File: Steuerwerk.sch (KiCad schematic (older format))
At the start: 130 parts, among them J1 2PinTerminalBlocktg, J10 2PinTerminalBlocktg, J11 2PinTerminalBlocktg, J12 2PinTerminalBlocktg, J2 2PinTerminalBlocktg, J3 3PinTerminalBlocktg, J4 3PinTerminalBlocktg, J5 2PinTerminalBlocktg, J6 2PinTerminalBlocktg, J7 2PinTerminalBlocktg, J8 2PinTerminalBlocktg, J9 2PinTerminalBlocktg, Q1 Q_PNP_BCE, U1 74ls240, U2 74541, U3 74LS161, U4 74LS138, U5 74LS138, U6 74541, U7 74LS374, U8 74LS374

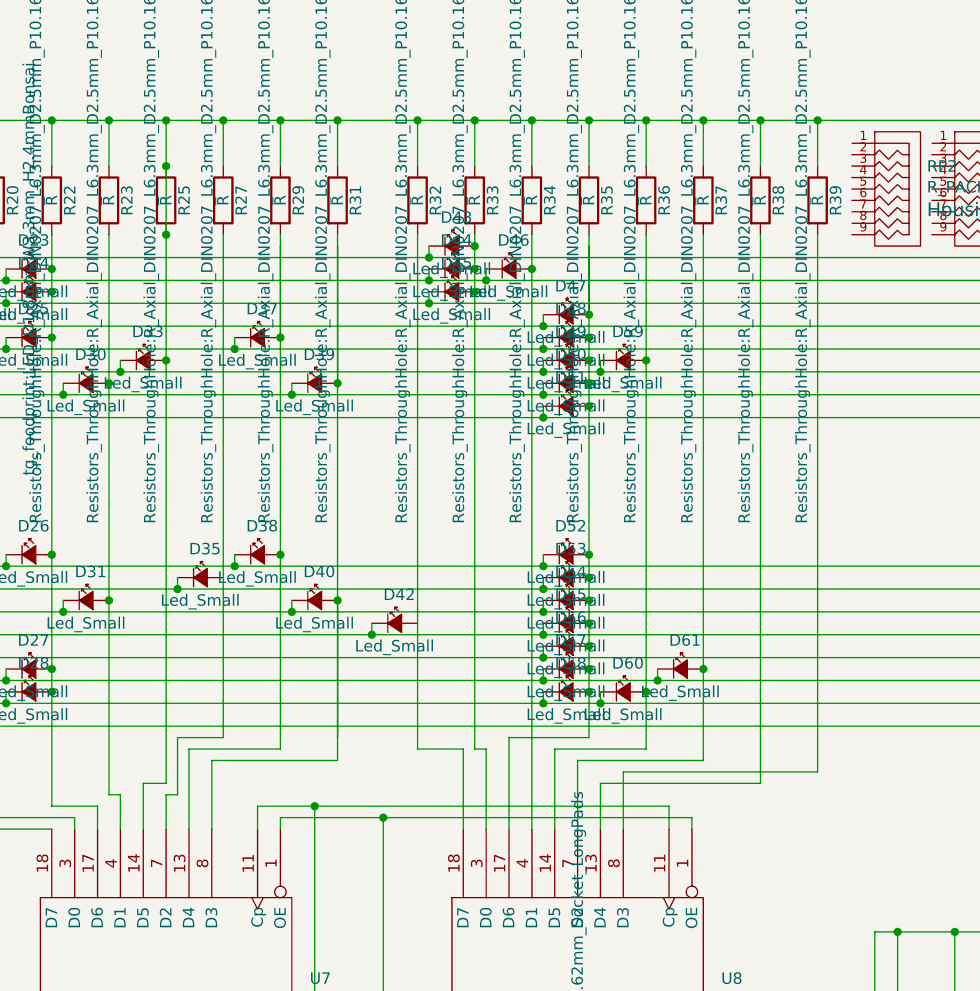
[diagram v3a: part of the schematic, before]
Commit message: Pin Anordnung von 374 korrigiert, manche Fehler gefunden und Todo Liste erweitert
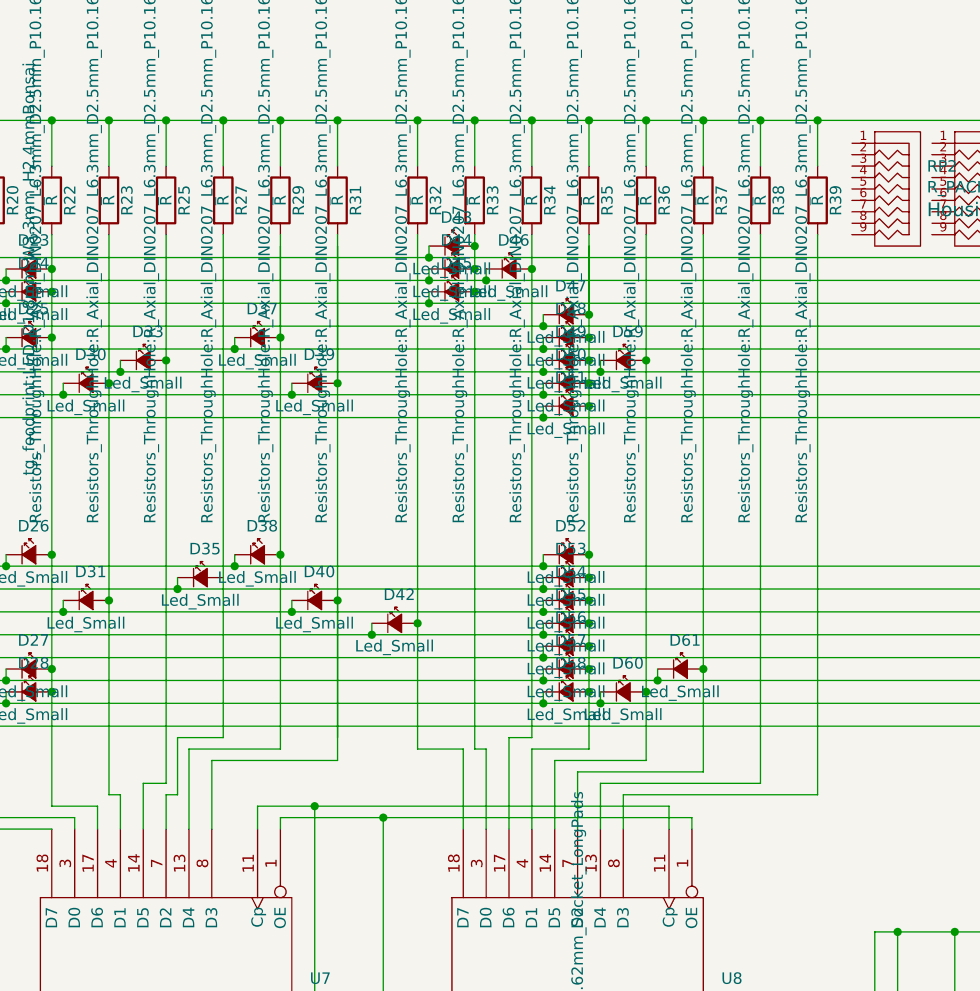
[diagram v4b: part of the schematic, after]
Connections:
- wire segments 441 -> 442
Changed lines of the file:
@@
 	8550 1000 8550 3400
-Wire Wire Line
-	7750 3300 8300 3300
-Wire Wire Line
-	8050 3250 7650 3250
-Wire Wire Line
-	7450 3200 7800 3200
 Wire Wire Line
 	6700 3300 6150 3300
@@
 	6000 2500 6000 2550
 Wire Wire Line
-	8800 1000 8800 3350
-Wire Wire Line
 	5200 1000 5200 1050
 Connection ~ 5200 500
@@
 	3550 700  3550 1100
 Wire Wire Line
-	7950 3350 8800 3350
+	7950 3450 8800 3450
 Wire Wire Line
 	8100 2950 11150 2950
@@
 	7950 5000 7950 6100
 Wire Wire Line
-	7950 3350 7950 3600
-Wire Wire Line
-	7750 3300 7750 3600
-Wire Wire Line
-	7650 3250 7650 3600
-Wire Wire Line
-	7450 3200 7450 3600
-Wire Wire Line
-	7250 3550 7250 3600
-Wire Wire Line
-	7250 3550 7250 3250
-Wire Wire Line
 	7250 3250 7050 3250
 Wire Wire Line
@@
 	6600 3550 6900 3550
 Wire Wire Line
-	7250 3550 8250 3550
-Wire Wire Line
 	6900 5250 6900 3550
 Wire Wire Line
 	1500 5250 6900 5250
-Connection ~ 6900 3550
-Wire Wire Line
-	6900 3550 7250 3550
 Connection ~ 1500 5250
 Wire Wire Line
@@
 Wire Wire Line
 	1050 5250 1500 5250
-Wire Wire Line
-	7050 1000 7050 3250
 Wire Wire Line
 	6200 1000 6200 3200
@@
 Wire Wire Line
 	5700 2600 5700 3450
-Connection ~ 5950 700
-Connection ~ 5950 1000
-Wire Wire Line
-	5950 1000 5950 700
 Wire Wire Line
 	5950 1550 5950 3400
@@
 	6700 1000 6700 1650
 Wire Wire Line
-	7550 1150 7550 3600
+	7550 1150 7550 3200
 Connection ~ 7800 2400
 Wire Wire Line
@@
 Connection ~ 7800 3000
 Wire Wire Line
-	7800 3000 7800 3200
-Wire Wire Line
 	8050 1000 8050 1550
 Connection ~ 8050 1550
@@
 Connection ~ 8050 3000
 Wire Wire Line
-	8050 3000 8050 3250
-Wire Wire Line
 	7800 1050 7800 1350
 Wire Wire Line
@@
 	7800 1000 7800 1350
 Connection ~ 8300 2900
-Wire Wire Line
-	8300 2900 8300 3300
 Connection ~ 7550 1150
 Wire Wire Line
@@
 	1    0    0    -1
 $EndComp
+Wire Wire Line
+	7550 3200 7450 3200
+Wire Wire Line
+	7450 3200 7450 3600
+Wire Wire Line
+	7950 3450 7950 3600
+Wire Wire Line
+	8800 1000 8800 3450
+Wire Wire Line
+	8300 3350 7750 3350
+Wire Wire Line
+	7750 3350 7750 3600
+Wire Wire Line
+	8300 2900 8300 3350
+Wire Wire Line
+	8050 3300 7650 3300
+Wire Wire Line
+	7650 3300 7650 3600
+Wire Wire Line
+	8050 3000 8050 3300
+Wire Wire Line
+	7800 3250 7550 3250
+Wire Wire Line
+	7550 3250 7550 3600
+Wire Wire Line
+	7800 3000 7800 3250
+Wire Wire Line
+	7050 1000 7050 2700
+Connection ~ 7050 2700
+Wire Wire Line
+	7050 2700 7050 3250
+Connection ~ 6900 3550
+Wire Wire Line
+	6900 3550 7250 3550
+Wire Wire Line
+	7250 3550 8250 3550
+Wire Wire Line
+	7250 3250 7250 3600
 $EndSCHEMATC

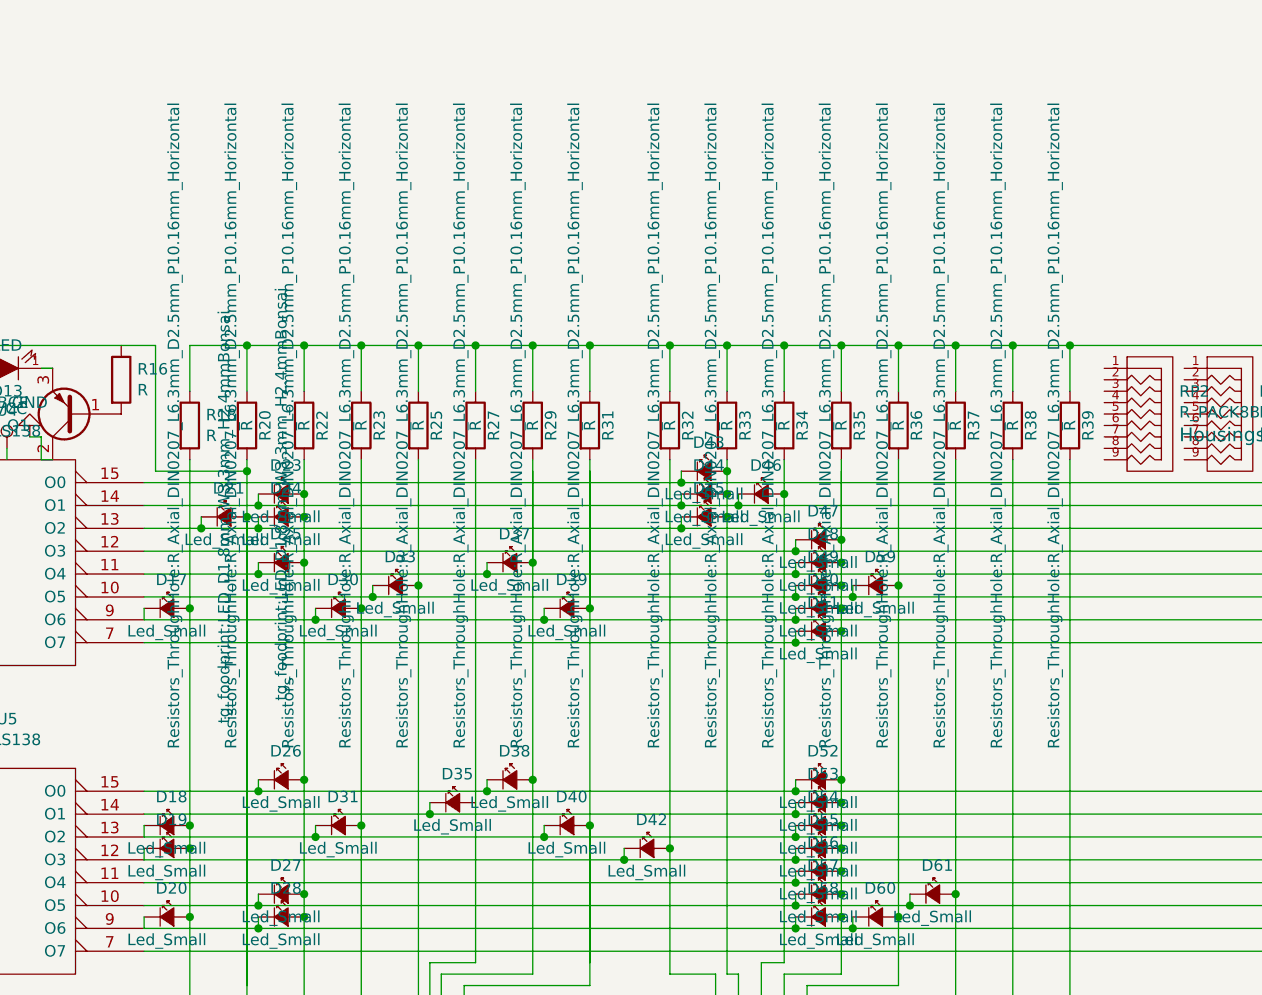
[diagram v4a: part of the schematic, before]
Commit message: Überflüssige LEDs entfernt, 1k Resistoren Eingebaut, Teile geordnet
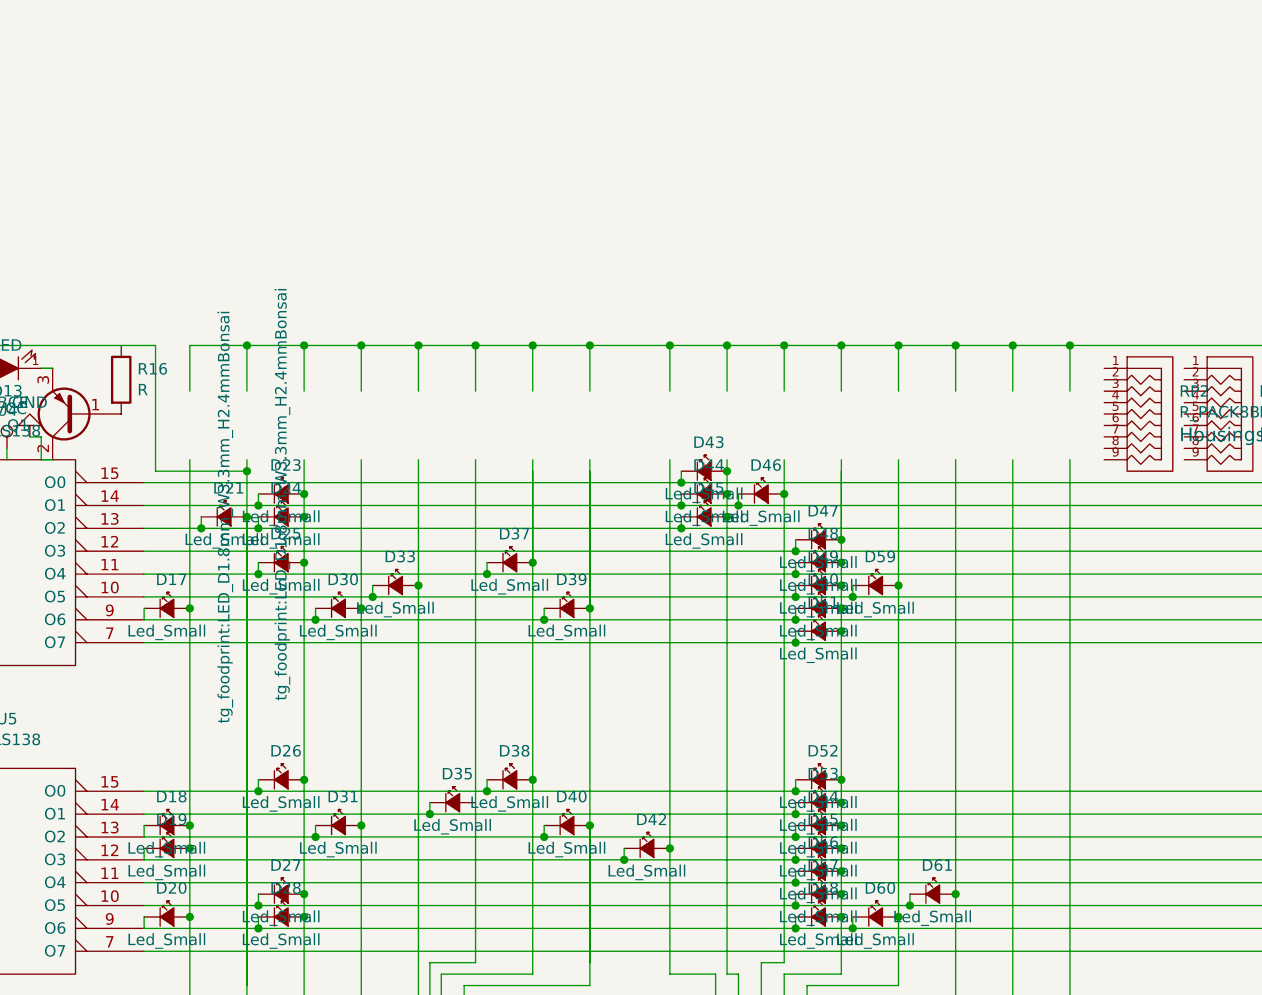
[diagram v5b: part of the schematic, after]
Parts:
- removed R18, R20, R22, R23, R25, R27, R29, R31, R32, R33, R34, R35, R36, R37, R38, R39: R, Resistors_ThroughHole:R_Axial_DIN0207_L6.3mm_D2.5mm_P10.16mm_Horizontal, symbol device:R
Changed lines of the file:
@@
-$EndComp
-$Comp
-L device:R R18
-U 1 1 57E93FB0
-P 4950 850
-F 0 "R18" H 5020 896 50  0000 L CNN
-F 1 "R" H 5020 805 50  0000 L CNN
-F 2 "Resistors_ThroughHole:R_Axial_DIN0207_L6.3mm_D2.5mm_P10.16mm_Horizontal" V 4880 850 50  0000 C CNN
-F 3 "" H 4950 850 50  0000 C CNN
-	1    4950 850
-	1    0    0    -1
 $EndComp
 $Comp
@@
 	1    0    0    -1
 $EndComp
-$Comp
-L device:R R20
-U 1 1 58344628
-P 5200 850
-F 0 "R20" V 5280 850 50  0000 C CNN
-F 1 "R" V 5200 850 50  0000 C CNN
-F 2 "Resistors_ThroughHole:R_Axial_DIN0207_L6.3mm_D2.5mm_P10.16mm_Horizontal" V 5130 850 50  0000 C CNN
-F 3 "" H 5200 850 50  0000 C CNN
-	1    5200 850
-	1    0    0    -1
-$EndComp
-$Comp
-L device:R R22
-U 1 1 583447D3
-P 5450 850
-F 0 "R22" V 5530 850 50  0000 C CNN
-F 1 "R" V 5450 850 50  0000 C CNN
-F 2 "Resistors_ThroughHole:R_Axial_DIN0207_L6.3mm_D2.5mm_P10.16mm_Horizontal" V 5380 850 50  0000 C CNN
-F 3 "" H 5450 850 50  0000 C CNN
-	1    5450 850
-	1    0    0    -1
-$EndComp
-$Comp
-L device:R R23
-U 1 1 58344948
-P 5700 850
-F 0 "R23" V 5780 850 50  0000 C CNN
-F 1 "R" V 5700 850 50  0000 C CNN
-F 2 "Resistors_ThroughHole:R_Axial_DIN0207_L6.3mm_D2.5mm_P10.16mm_Horizontal" V 5630 850 50  0000 C CNN
-F 3 "" H 5700 850 50  0000 C CNN
-	1    5700 850
-	1    0    0    -1
-$EndComp
-$Comp
-L device:R R25
-U 1 1 58344ABE
-P 5950 850
-F 0 "R25" V 6030 850 50  0000 C CNN
-F 1 "R" V 5950 850 50  0000 C CNN
-F 2 "Resistors_ThroughHole:R_Axial_DIN0207_L6.3mm_D2.5mm_P10.16mm_Horizontal" V 5880 850 50  0000 C CNN
-F 3 "" H 5950 850 50  0000 C CNN
-	1    5950 850
-	1    0    0    -1
-$EndComp
-$Comp
-L device:R R27
-U 1 1 58344C33
-P 6200 850
-F 0 "R27" V 6280 850 50  0000 C CNN
-F 1 "R" V 6200 850 50  0000 C CNN
-F 2 "Resistors_ThroughHole:R_Axial_DIN0207_L6.3mm_D2.5mm_P10.16mm_Horizontal" V 6130 850 50  0000 C CNN
-F 3 "" H 6200 850 50  0000 C CNN
-	1    6200 850
-	1    0    0    -1
-$EndComp
-$Comp
-L device:R R29
-U 1 1 5834A44B
-P 6450 850
-F 0 "R29" V 6530 850 50  0000 C CNN
-F 1 "R" V 6450 850 50  0000 C CNN
-F 2 "Resistors_ThroughHole:R_Axial_DIN0207_L6.3mm_D2.5mm_P10.16mm_Horizontal" V 6380 850 50  0000 C CNN
-F 3 "" H 6450 850 50  0000 C CNN
-	1    6450 850
-	1    0    0    -1
-$EndComp
-$Comp
-L device:R R31
-U 1 1 5834A548
-P 6700 850
-F 0 "R31" V 6780 850 50  0000 C CNN
-F 1 "R" V 6700 850 50  0000 C CNN
-F 2 "Resistors_ThroughHole:R_Axial_DIN0207_L6.3mm_D2.5mm_P10.16mm_Horizontal" V 6630 850 50  0000 C CNN
-F 3 "" H 6700 850 50  0000 C CNN
-	1    6700 850
-	1    0    0    -1
-$EndComp
-$Comp
-L device:R R32
-U 1 1 58350BA0
-P 7050 850
-F 0 "R32" V 7130 850 50  0000 C CNN
-F 1 "R" V 7050 850 50  0000 C CNN
-F 2 "Resistors_ThroughHole:R_Axial_DIN0207_L6.3mm_D2.5mm_P10.16mm_Horizontal" V 6980 850 50  0000 C CNN
-F 3 "" H 7050 850 50  0000 C CNN
-	1    7050 850
-	1    0    0    -1
-$EndComp
-$Comp
-L device:R R33
-U 1 1 58350CC5
-P 7300 850
-F 0 "R33" V 7380 850 50  0000 C CNN
-F 1 "R" V 7300 850 50  0000 C CNN
-F 2 "Resistors_ThroughHole:R_Axial_DIN0207_L6.3mm_D2.5mm_P10.16mm_Horizontal" V 7230 850 50  0000 C CNN
-F 3 "" H 7300 850 50  0000 C CNN
-	1    7300 850
-	1    0    0    -1
-$EndComp
-$Comp
-L device:R R34
-U 1 1 58350F70
-P 7550 850
-F 0 "R34" V 7630 850 50  0000 C CNN
-F 1 "R" V 7550 850 50  0000 C CNN
-F 2 "Resistors_ThroughHole:R_Axial_DIN0207_L6.3mm_D2.5mm_P10.16mm_Horizontal" V 7480 850 50  0000 C CNN
-F 3 "" H 7550 850 50  0000 C CNN
-	1    7550 850
-	1    0    0    -1
-$EndComp
-$Comp
-L device:R R35
-U 1 1 58351097
-P 7800 850
-F 0 "R35" V 7880 850 50  0000 C CNN
-F 1 "R" V 7800 850 50  0000 C CNN
-F 2 "Resistors_ThroughHole:R_Axial_DIN0207_L6.3mm_D2.5mm_P10.16mm_Horizontal" V 7730 850 50  0000 C CNN
-F 3 "" H 7800 850 50  0000 C CNN
-	1    7800 850
-	1    0    0    -1
-$EndComp
-$Comp
-L device:R R36
-U 1 1 583511A4
-P 8050 850
-F 0 "R36" V 8130 850 50  0000 C CNN
-F 1 "R" V 8050 850 50  0000 C CNN
-F 2 "Resistors_ThroughHole:R_Axial_DIN0207_L6.3mm_D2.5mm_P10.16mm_Horizontal" V 7980 850 50  0000 C CNN
-F 3 "" H 8050 850 50  0000 C CNN
-	1    8050 850
-	1    0    0    -1
-$EndComp
-$Comp
-L device:R R37
-U 1 1 583512C3
-P 8300 850
-F 0 "R37" V 8380 850 50  0000 C CNN
-F 1 "R" V 8300 850 50  0000 C CNN
-F 2 "Resistors_ThroughHole:R_Axial_DIN0207_L6.3mm_D2.5mm_P10.16mm_Horizontal" V 8230 850 50  0000 C CNN
-F 3 "" H 8300 850 50  0000 C CNN
-	1    8300 850
-	1    0    0    -1
-$EndComp
-$Comp
-L device:R R38
-U 1 1 583513E8
-P 8550 850
-F 0 "R38" V 8630 850 50  0000 C CNN
-F 1 "R" V 8550 850 50  0000 C CNN
-F 2 "Resistors_ThroughHole:R_Axial_DIN0207_L6.3mm_D2.5mm_P10.16mm_Horizontal" V 8480 850 50  0000 C CNN
-F 3 "" H 8550 850 50  0000 C CNN
-	1    8550 850
-	1    0    0    -1
-$EndComp
-$Comp
-L device:R R39
-U 1 1 5835158D
-P 8800 850
-F 0 "R39" V 8880 850 50  0000 C CNN
-F 1 "R" V 8800 850 50  0000 C CNN
-F 2 "Resistors_ThroughHole:R_Axial_DIN0207_L6.3mm_D2.5mm_P10.16mm_Horizontal" V 8730 850 50  0000 C CNN
-F 3 "" H 8800 850 50  0000 C CNN
-	1    8800 850
-	1    0    0    -1
-$EndComp

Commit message: Steuerwerk: a lot of things ...
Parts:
- added D63: Led_Small, tg_foodprint:LED_D1.8mm_W3.3mm_H2.4mmBonsai, symbol device:LED_Small
- U8: footprint Housings_DIP:DIP-20_W7.62mm_Socket_LongPads -> tg_foodprint:DIP-20_W7.62mm_Socket_LongPadstg
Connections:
- net labels added: a1, a2, a3, a4, a5, a6, a7, a8, b1, b2, b3, b4, b5, b6, b7, b8
- net labels removed: vom_Befehle-decoder
- wire segments 442 -> 414
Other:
- note added: "vom_Befehle-decoder"
- moved on the sheet: D60, D61, RP1, RP2

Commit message: steuerwerk improvements
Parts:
- removed U1: 74ls240, Housings_DIP:DIP-20_W7.62mm_Socket_LongPads, symbol bonsai:74ls240
- added U9: 74ls240, Package_DIP:DIP-20_W7.62mm_Socket_LongPads, symbol bonsai:74ls240
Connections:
- wire segments 414 -> 424
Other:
- moved on the sheet: D1, D10, D4, D6, D8, R1, R10, R4, R6, R8

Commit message: tracs tracs tracs
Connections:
- wire segments 424 -> 422
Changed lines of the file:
@@
 Connection ~ 3200 2950
-Wire Wire Line
-	3350 1800 3550 1800
 Wire Wire Line
 	3350 700  3550 700
@@
 	3100 700  3350 700
 Connection ~ 3350 700
-Wire Wire Line
-	3350 700  3350 1800
 Connection ~ 3350 2450
-Wire Wire Line
-	3350 1800 3350 2450
-Wire Wire Line
-	3200 1000 3200 1800
-Wire Wire Line
-	3200 1800 3200 2950
-Connection ~ 3200 1800
-Wire Wire Line
-	3350 1800 3200 1800
 Connection ~ 1600 6700
 Wire Wire Line
@@
 Wire Wire Line
 	2500 6700 2550 6700
+Connection ~ 2550 6700
+Wire Wire Line
+	3200 1000 3200 1800
+Wire Wire Line
+	3350 700  3350 2450
+Wire Wire Line
+	3550 1800 3200 1800
 Wire Bus Line
 	4850 900  6600 900
 Wire Bus Line
 	6950 900  8700 900
-Connection ~ 2550 6700
+Connection ~ 3200 1800
+Wire Wire Line
+	3200 1800 3200 2950
 $EndSCHEMATC
